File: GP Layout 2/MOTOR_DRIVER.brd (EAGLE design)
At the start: 91.4 x 97.5 mm, 54 parts, among them U7 ATMEGA328P_TQFP, Y1 16MHz

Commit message: ISCP connectors
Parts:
- removed TXRX: (no value), con-lsta:FE02-1
- added PROGRAM: (no value), arduino_jw:CONN-2X03
- R1: value 9090 -> 2800
- R2: value 4750 -> 1620
- R3: value 2.32M -> 2320
- R4: value 1.15M -> 1150
- moved SV2 1.60 mm to (23.2, 3.81)
- moved C12 0.28 mm to (59.4, 91.7)
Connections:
- net RX: no longer TXRX.1
- net TX: no longer TXRX.2
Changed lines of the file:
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@@
 <attribute name="MF" value="" x="21.59" y="40.64" size="1.778" layer="27" display="off"/>
 </element>
-<element name="SV2" library="con-lsta" package="FE10" value="" x="21.59" y="3.81">
-<attribute name="OC_FARNELL" value="unknown" x="21.59" y="3.81" size="1.778" layer="27" display="off"/>
-<attribute name="MPN" value="" x="21.59" y="3.81" size="1.778" layer="27" display="off"/>
-<attribute name="OC_NEWARK" value="unknown" x="21.59" y="3.81" size="1.778" layer="27" display="off"/>
-<attribute name="MF" value="" x="21.59" y="3.81" size="1.778" layer="27" display="off"/>
+<element name="SV2" library="con-lsta" package="FE10" value="" x="23.19" y="3.81">
+<attribute name="OC_FARNELL" value="unknown" x="23.19" y="3.81" size="1.778" layer="27" display="off"/>
+<attribute name="MPN" value="" x="23.19" y="3.81" size="1.778" layer="27" display="off"/>
+<attribute name="OC_NEWARK" value="unknown" x="23.19" y="3.81" size="1.778" layer="27" display="off"/>
+<attribute name="MF" value="" x="23.19" y="3.81" size="1.778" layer="27" display="off"/>
 </element>
 <element name="SV5" library="con-lsta" package="FE10" value="" x="24.542" y="94.28">
@@
 <element name="BATT_LOW" library="solpad" package="SE14" value="SE14" x="3.87" y="72.21"/>
 <element name="C8" library="resistor" package="C050-025X075" value="10uF" x="42.196" y="36.492"/>
-<element name="C12" library="resistor" package="153CLV-1010" value="" x="59.566" y="91.9"/>
+<element name="C12" library="resistor" package="153CLV-1010" value="" x="59.366" y="91.7"/>
 <element name="C13" library="resistor" package="153CLV-1010" value="" x="59.358" y="80.662"/>
 <element name="C14" library="resistor" package="153CLV-1010" value="" x="59.766" y="69.3"/>
@@
 <element name="FUSE" library="minifuse" package="FUSEHOLDER3588" value="" x="15.548" y="73.816"/>
 <element name="BIG_SWITCH" library="bigswitch" package="BIGSWITCH" value="" x="3.158" y="83.06" rot="R90"/>
-<element name="R1" library="SparkFun-Resistors" package="0805" value="9090" x="31.158" y="23.49">
+<element name="R1" library="SparkFun-Resistors" package="0805" value="2800" x="31.158" y="23.49">
 <attribute name="PROD_ID" value="RES-11622" x="31.158" y="23.49" size="1.778" layer="27" display="off"/>
 </element>
-<element name="R2" library="SparkFun-Resistors" package="0805" value="4750" x="27.202" y="23.49">
+<element name="R2" library="SparkFun-Resistors" package="0805" value="1620" x="27.202" y="23.49">
 <attribute name="PROD_ID" value="RES-11622" x="27.202" y="23.49" size="1.778" layer="27" display="off"/>
 </element>
-<element name="R3" library="SparkFun-Resistors" package="0805" value="2.32M" x="23.346" y="23.49">
+<element name="R3" library="SparkFun-Resistors" package="0805" value="2320" x="23.346" y="23.49">
 <attribute name="PROD_ID" value="RES-11622" x="23.346" y="23.49" size="1.778" layer="27" display="off"/>
 </element>
-<element name="R4" library="SparkFun-Resistors" package="0805" value="1.15M" x="19.59" y="23.49">
+<element name="R4" library="SparkFun-Resistors" package="0805" value="1150" x="19.59" y="23.49">
 <attribute name="PROD_ID" value="RES-11622" x="19.59" y="23.49" size="1.778" layer="27" display="off"/>
 </element>
@@
 <attribute name="MF" value="" x="83.126" y="30.082" size="1.778" layer="27" display="off"/>
 </element>
-<element name="TXRX" library="con-lsta" package="FE02-1" value="" x="9.05" y="3.758"/>
 <element name="MOTOR_NEG_B" library="solpad" package="SE14" value="SE14" x="3.9" y="55.2"/>
 <element name="TGPIO" library="con-lsta" package="FE09" value="" x="56.4" y="32.4" rot="R180">
@@
 <attribute name="MF" value="" x="56.4" y="32.4" size="1.778" layer="27" rot="R180" display="off"/>
 </element>
+<element name="PROGRAM" library="arduino_jw" package="CONN-2X03" value="" x="-43.7" y="-17"/>
 </elements>
 <signals>
@@
 <contactref element="R3" pad="2"/>
 <contactref element="SV2" pad="5"/>
-<wire x1="20.32" y1="3.81" x2="24.246" y2="23.49" width="0" layer="19" extent="1-1"/>
+<wire x1="21.92" y1="3.81" x2="24.246" y2="23.49" width="0" layer="19" extent="1-1"/>
 </signal>
 <signal name="N$2">
@@
 <contactref element="SV2" pad="6"/>
 <contactref element="S1" pad="8"/>
-<wire x1="22.86" y1="3.81" x2="18.69" y2="23.49" width="0" layer="19" extent="1-1"/>
-<wire x1="51.82" y1="10.4758" x2="22.86" y2="3.81" width="0" layer="19" extent="1-1"/>
+<wire x1="24.46" y1="3.81" x2="18.69" y2="23.49" width="0" layer="19" extent="1-1"/>
+<wire x1="51.82" y1="10.4758" x2="24.46" y2="3.81" width="0" layer="19" extent="1-1"/>
 </signal>
 <signal name="N$9">
@@
 <signal name="RX">
 <contactref element="U7" pad="30"/>
-<contactref element="TXRX" pad="1"/>
-<wire x1="3.97" y1="3.758" x2="59.722" y2="25.8106" width="0" layer="19" extent="1-1"/>
 </signal>
 <signal name="TX">
 <contactref element="U7" pad="31"/>
-<contactref element="TXRX" pad="2"/>
-<wire x1="6.51" y1="3.758" x2="58.922" y2="25.8106" width="0" layer="19" extent="1-1"/>
 </signal>
 <signal name="5V">
@@
 <wire x1="12.64" y1="66.24" x2="26.245" y2="71.6757" width="0" layer="19" extent="16-16"/>
 <wire x1="3.87" y1="72.21" x2="12.64" y2="66.24" width="0" layer="19" extent="1-1"/>
-<wire x1="55.566" y1="91.9" x2="3.87" y2="72.21" width="0" layer="19" extent="1-1"/>
-<wire x1="55.358" y1="80.662" x2="55.566" y2="91.9" width="0" layer="19" extent="1-1"/>
+<wire x1="55.366" y1="91.7" x2="3.87" y2="72.21" width="0" layer="19" extent="1-1"/>
+<wire x1="55.358" y1="80.662" x2="55.366" y2="91.7" width="0" layer="19" extent="1-1"/>
 <wire x1="55.766" y1="69.3" x2="55.358" y2="80.662" width="0" layer="19" extent="1-1"/>
 <wire x1="55.666" y1="57.9" x2="55.766" y2="69.3" width="0" layer="19" extent="1-1"/>
@@
 <wire x1="63.766" y1="69.3" x2="63.666" y2="57.9" width="0" layer="19" extent="1-1"/>
 <wire x1="63.358" y1="80.662" x2="63.766" y2="69.3" width="0" layer="19" extent="1-1"/>
-<wire x1="63.566" y1="91.9" x2="63.358" y2="80.662" width="0" layer="19" extent="1-1"/>
+<wire x1="63.366" y1="91.7" x2="63.358" y2="80.662" width="0" layer="19" extent="1-1"/>
 </signal>
 <signal name="BATT_VOLTAGE_SENSE">
@@
 <contactref element="U$1" pad="3/CANTX"/>
 <contactref element="SV2" pad="1"/>
-<wire x1="10.16" y1="3.81" x2="18.324" y2="13.698" width="0" layer="19" extent="1-1"/>
+<wire x1="11.76" y1="3.81" x2="18.324" y2="13.698" width="0" layer="19" extent="1-1"/>
 </signal>
 <signal name="LI1">
 <contactref element="U$1" pad="4/CANRX"/>
 <contactref element="SV2" pad="2"/>
-<wire x1="12.7" y1="3.81" x2="20.864" y2="13.698" width="0" layer="19" extent="1-1"/>
+<wire x1="14.3" y1="3.81" x2="20.864" y2="13.698" width="0" layer="19" extent="1-1"/>
 </signal>
 <signal name="LI1_TOP">
@@
 <contactref element="U$1" pad="5"/>
 <contactref element="SV2" pad="3"/>
-<wire x1="15.24" y1="3.81" x2="23.404" y2="13.698" width="0" layer="19" extent="1-1"/>
+<wire x1="16.84" y1="3.81" x2="23.404" y2="13.698" width="0" layer="19" extent="1-1"/>
 </signal>
 <signal name="LI2">
 <contactref element="U$1" pad="6"/>
 <contactref element="SV2" pad="4"/>
-<wire x1="17.78" y1="3.81" x2="25.944" y2="13.698" width="0" layer="19" extent="1-1"/>
+<wire x1="19.38" y1="3.81" x2="25.944" y2="13.698" width="0" layer="19" extent="1-1"/>
 </signal>
 <signal name="HI2_TOP">

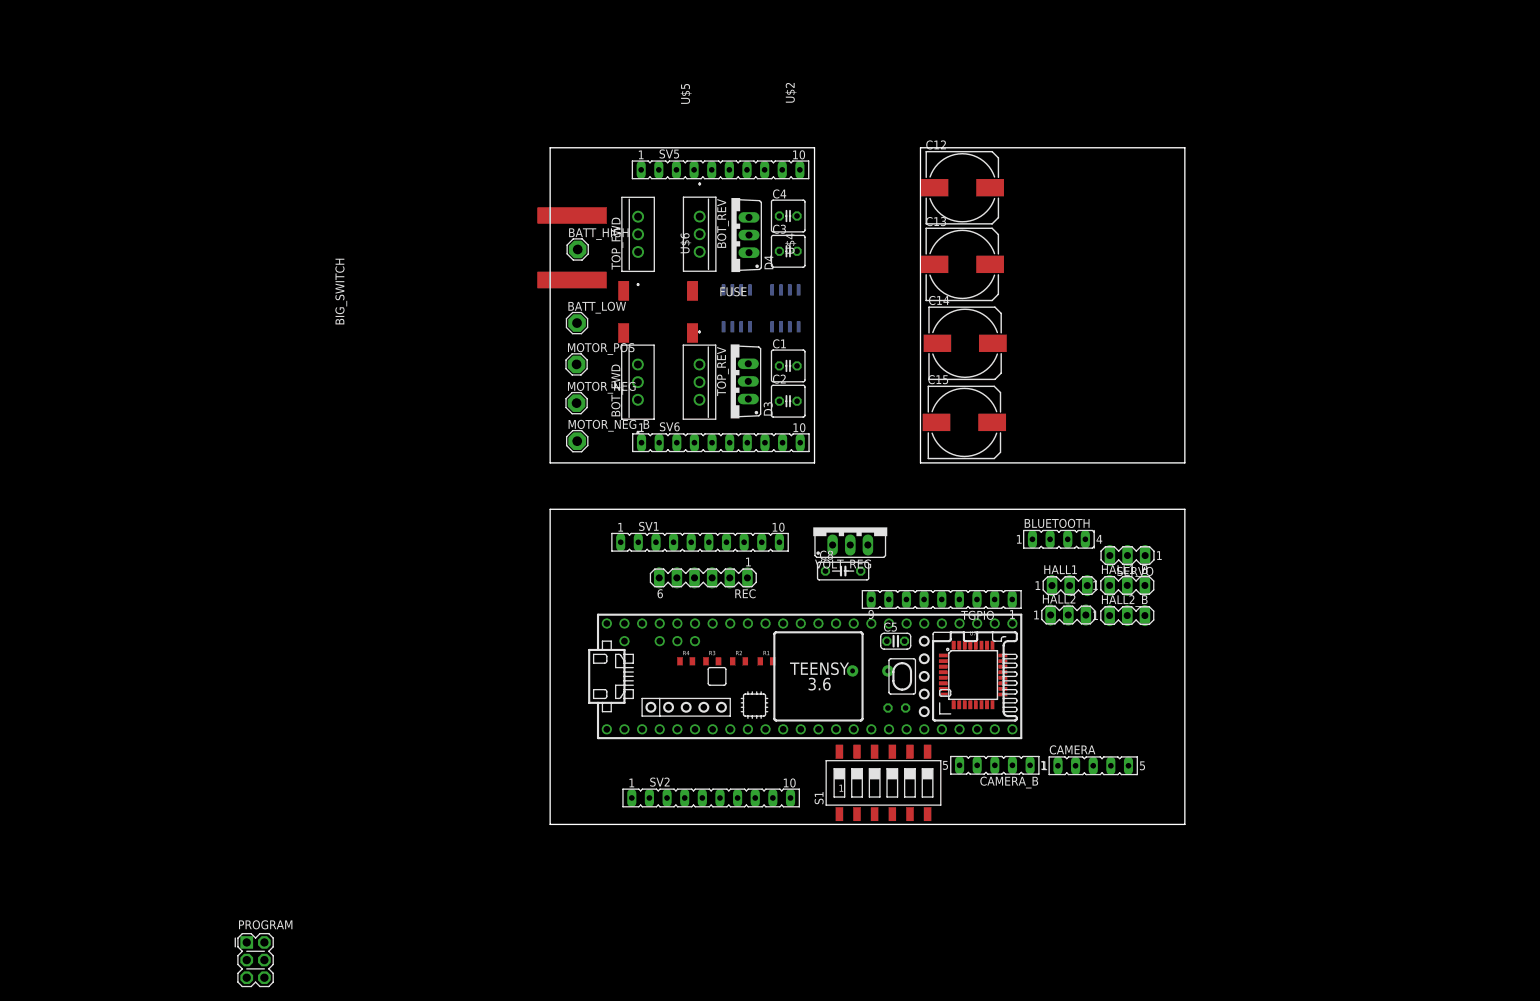
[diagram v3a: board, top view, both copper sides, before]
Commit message: added led driver, indicator leds, etc
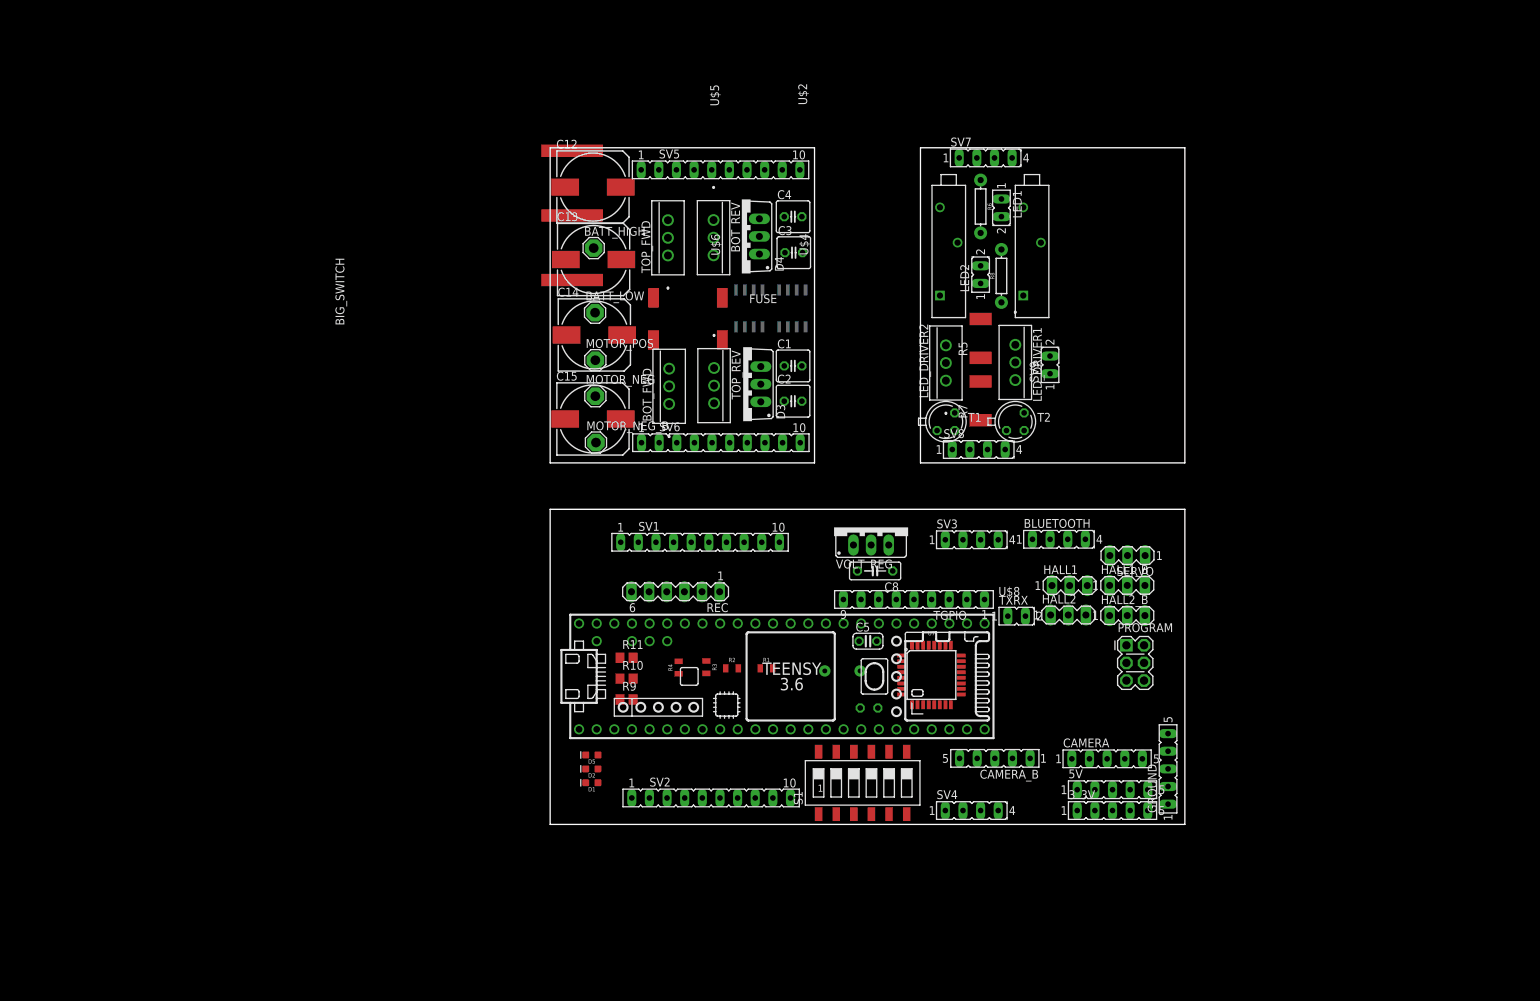
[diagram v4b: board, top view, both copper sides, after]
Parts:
- added 3_3V, 5V, GROUND: (no value), con-lsta:FE05-1
- added D1, D2, D5: (no value), SparkFun-LED:LED-0603
- added LED1, LED2, SV9, TXRX: (no value), con-lsta:FE02-1
- added LED_DRIVER1, LED_DRIVER2: CSD18502KCS_KCS_3, CSD18502KCS:KCS3
- added R10, R11, R9: (no value), rcl:R0805
- added R5, R7: (no value), rcl:R2512
- added R6, R8: 1k, SparkFun-Resistors:AXIAL-0.3
- added SV3, SV4, SV7, SV8: (no value), con-lsta:FE04-1
- added T1, T2: 2N2222, transistor:TO18
- added U$3, U$7: POT, ledpot:POT
- added U$8: (no value), heatsink:HEATSINK
- moved PROGRAM 133.7 mm to (83.0, 25.8)
- moved C15 53.5 mm to (6.17, 58.4)
- moved C14 53.4 mm to (6.37, 70.5)
- moved C12 53.2 mm to (6.17, 91.8)
- moved C13 53.1 mm to (6.26, 81.4)
- moved U7 6.00 mm to (54.9, 21.5)
- moved C8 4.61 mm to (46.8, 36.5), turned to 180 degrees
- moved BOT_FWD 4.54 mm to (17.1, 65.6)
- moved REC 4.47 mm to (18.1, 33.5)
- moved FUSE 4.41 mm to (19.8, 72.8)
- moved U$6 4.40 mm to (13.4, 63.4)
- moved TOP_FWD 4.33 mm to (17.0, 87.0)
- moved U$5 4.20 mm to (13.3, 84.9)
- moved C5 4.00 mm to (45.8, 26.4)
- moved C6 4.00 mm to (45.9, 16.8)
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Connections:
- net N$13 renamed SPI_SS
- new net 7_4V_TOP2: LED1.2, LED2.2, R6.P$2, R8.P$2, SV9.2
- new net GND_TOP2: SV9.1, T1.1, T2.1, U$3.P2, U$7.P2
- new net N$1: R5.1, U$7.P3
- new net N$13: R7.1, U$3.P3
- new net N$14: PROGRAM.5
- new net N$17: LED1.1, LED_DRIVER2.2
- new net N$19: LED_DRIVER1.1, R8.P$1, T2.3
- new net N$20: LED2.1, LED_DRIVER1.2
- new net N$22: D1.A, R9.1
- new net N$23: D2.A, R10.1
- new net N$24: D5.A, R11.1
- new net N$8: LED_DRIVER2.3, R5.2, T1.2
- new net SPI_MISO: PROGRAM.1, U$1.11/MOSI, U7.16
- new net SPI_MOSI: PROGRAM.4, U$1.12/MISO, U7.15
- new net SPI_SCK: PROGRAM.3, U$1.13/SCK, U7.17
- net 3_3V: now also 3_3V.1, 3_3V.2, 3_3V.3, 3_3V.4, 3_3V.5
- net 5V: now also 5V.1, 5V.2, 5V.3, 5V.4, 5V.5
- net 7_4V: now also SV1.7; no longer SV1.1
- net 7_4V_TOP: now also SV5.5, SV5.6, SV5.7, SV5.8; no longer SV5.1
- net GND: now also D1.C, D2.C, D5.C, GROUND.1, GROUND.2, GROUND.3, GROUND.4, GROUND.5
- net GND_TOP: now also SV5.1, SV5.2, SV5.3, SV5.4, SV5.9
- net LED1: now also R9.2
- net LED2: now also R10.2
- net LED3: now also R11.2
- net N$15: now also PROGRAM.6; no longer U$1.12/MISO, U7.15
- net N$16: now also LED_DRIVER2.1, R6.P$1, T1.3; no longer U$1.13/SCK, U7.17
- net N$18: now also LED_DRIVER1.3, R7.2, T2.2; no longer U$1.11/MOSI, U7.16
- net RX: now also TXRX.1
- net TX: now also TXRX.2

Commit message: double check
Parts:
- moved SERVO 1.00 mm to (83.2, 39.7)
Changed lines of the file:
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@@
 </element>
 <element name="BLUETOOTH" library="con-lsta" package="FE04-1" value="" x="74.55" y="41.066"/>
-<element name="SERVO" library="con-lstb" package="MA03-1" value="" x="83.158" y="38.726" rot="R180">
-<attribute name="MPN" value="" x="83.158" y="38.726" size="1.778" layer="27" rot="R180" display="off"/>
-<attribute name="OC_FARNELL" value="unknown" x="83.158" y="38.726" size="1.778" layer="27" rot="R180" display="off"/>
-<attribute name="OC_NEWARK" value="unknown" x="83.158" y="38.726" size="1.778" layer="27" rot="R180" display="off"/>
-<attribute name="MF" value="" x="83.158" y="38.726" size="1.778" layer="27" rot="R180" display="off"/>
+<element name="SERVO" library="con-lstb" package="MA03-1" value="" x="83.158" y="39.726" rot="R180">
+<attribute name="MPN" value="" x="83.158" y="39.726" size="1.778" layer="27" rot="R180" display="off"/>
+<attribute name="OC_FARNELL" value="unknown" x="83.158" y="39.726" size="1.778" layer="27" rot="R180" display="off"/>
+<attribute name="OC_NEWARK" value="unknown" x="83.158" y="39.726" size="1.778" layer="27" rot="R180" display="off"/>
+<attribute name="MF" value="" x="83.158" y="39.726" size="1.778" layer="27" rot="R180" display="off"/>
 </element>
 <element name="HALL1" library="con-lstb" package="MA03-1" value="" x="74.826" y="34.402">
@@
 <contactref element="D2" pad="C"/>
 <contactref element="D5" pad="C"/>
-<wire x1="83.126" y1="34.422" x2="85.698" y2="38.726" width="0" layer="19" extent="1-1"/>
+<wire x1="83.126" y1="34.422" x2="85.698" y2="39.726" width="0" layer="19" extent="1-1"/>
 <wire x1="83.126" y1="30.082" x2="83.126" y2="34.422" width="0" layer="19" extent="1-1"/>
 <wire x1="74.826" y1="34.402" x2="83.126" y2="34.422" width="0" layer="19" extent="1-1"/>
@@
 <contactref element="SERVO" pad="3"/>
 <contactref element="U$1" pad="9/CS"/>
-<wire x1="29.564" y1="13.698" x2="80.618" y2="38.726" width="0" layer="19" extent="1-1"/>
+<wire x1="29.564" y1="13.698" x2="80.618" y2="39.726" width="0" layer="19" extent="1-1"/>
 </signal>
 <signal name="BLT_RX">
@@
 <contactref element="5V" pad="2"/>
 <contactref element="5V" pad="1"/>
-<wire x1="49.344" y1="36.508" x2="83.158" y2="38.726" width="0" layer="19" extent="1-1"/>
+<wire x1="49.344" y1="36.508" x2="83.158" y2="39.726" width="0" layer="19" extent="1-1"/>
 <wire x1="46.226" y1="40.246" x2="49.344" y2="36.508" width="0" layer="19" extent="1-1"/>
 <wire x1="21.874" y1="33.51" x2="46.226" y2="40.246" width="0" layer="19" extent="1-1"/>
